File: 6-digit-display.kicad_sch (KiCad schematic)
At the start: 6 parts, among them U1 MAX7219, U2 3_digit_7_segment_display, U3 3_digit_7_segment_display

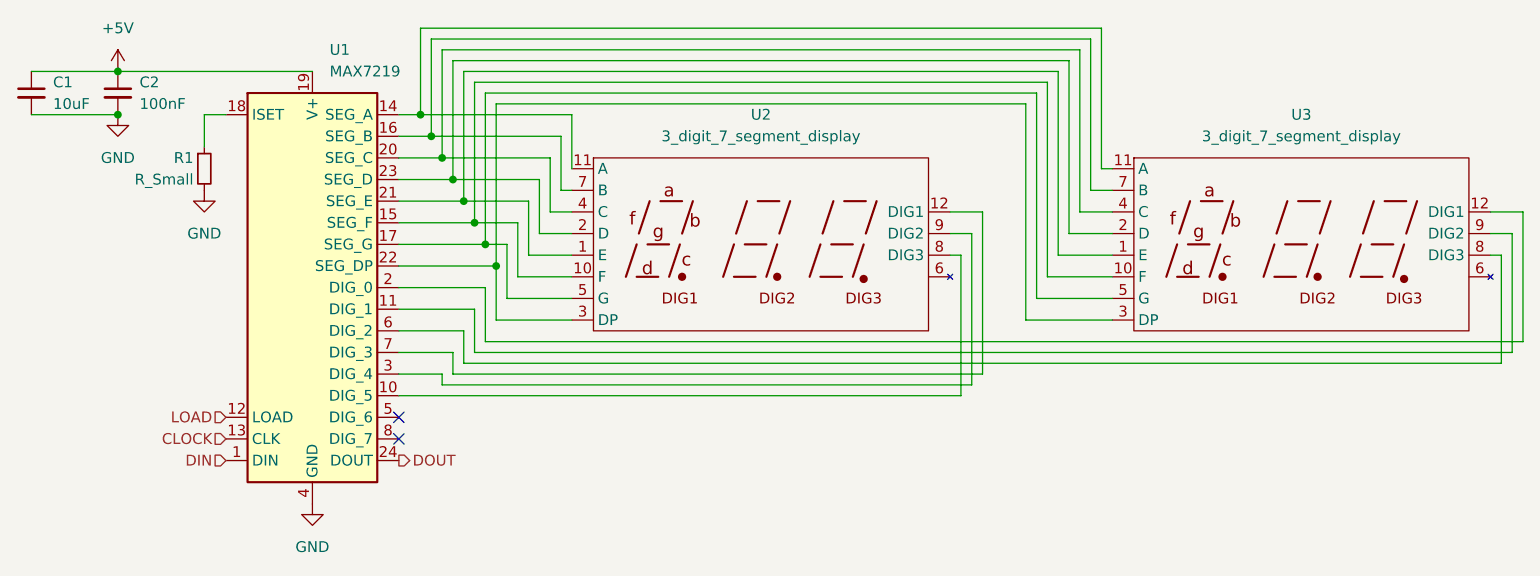
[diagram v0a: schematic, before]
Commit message: Add RP2040
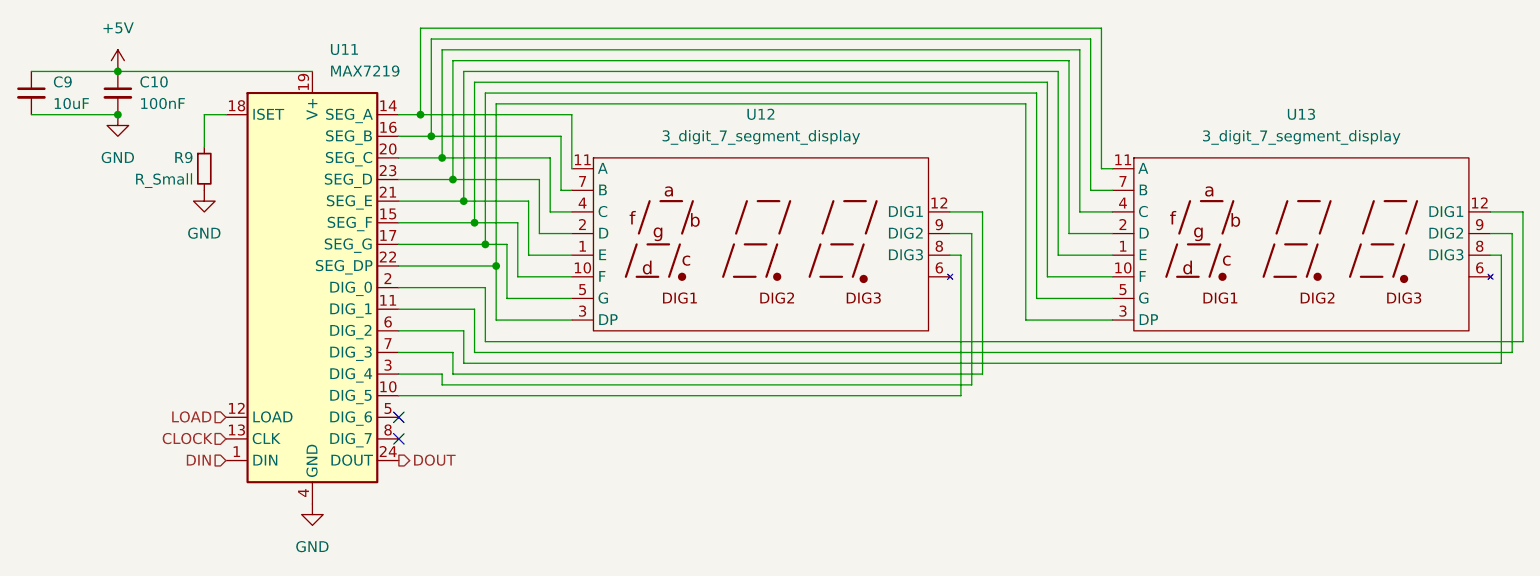
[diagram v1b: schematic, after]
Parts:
- renumbered C2 to C10, C1 to C9, R1 to R9, U1 to U11, U2 to U12, U3 to U13
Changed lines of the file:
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@@
   (symbol (lib_id "Driver_LED:MAX7219") (at 60.96 101.6 0)
     (in_bom yes) (on_board yes) (fields_autoplaced)
-    (property "Reference" "U1" (id 0) (at 62.9794 73.66 0)
+    (property "Reference" "U11" (id 0) (at 62.9794 73.66 0)
       (effects (font (size 1.27 1.27)) (justify left))
     )
@@
   (symbol (lib_id "Generic-radio-stack:3_digit_7_segment_display") (at 176.53 96.52 0)
     (in_bom yes) (on_board yes) (fields_autoplaced)
-    (property "Reference" "U3" (id 0) (at 177.165 81.28 0))
+    (property "Reference" "U13" (id 0) (at 177.165 81.28 0))
     (property "Value" "3_digit_7_segment_display" (id 1) (at 177.165 83.82 0))
     (property "Footprint" "" (id 2) (at 181.61 96.52 0)
@@
   (symbol (lib_id "Device:C_Small") (at 38.1 78.74 0)
     (in_bom yes) (on_board yes) (fields_autoplaced)
-    (property "Reference" "C2" (id 0) (at 40.64 77.4762 0)
+    (property "Reference" "C10" (id 0) (at 40.64 77.4762 0)
       (effects (font (size 1.27 1.27)) (justify left))
     )
@@
   (symbol (lib_id "power:GND") (at 38.1 81.28 0)
     (in_bom yes) (on_board yes) (fields_autoplaced)
-    (property "Reference" "#PWR014" (id 0) (at 38.1 87.63 0)
+    (property "Reference" "#PWR023" (id 0) (at 38.1 87.63 0)
       (effects (font (size 1.27 1.27)) hide)
     )
@@
   (symbol (lib_id "Device:R_Small") (at 48.26 87.63 0)
     (in_bom yes) (on_board yes)
-    (property "Reference" "R1" (id 0) (at 46.99 86.36 0)
+    (property "Reference" "R9" (id 0) (at 46.99 86.36 0)
       (effects (font (size 1.27 1.27)) (justify right))
     )
@@
   (symbol (lib_id "power:+5V") (at 38.1 76.2 0)
     (in_bom yes) (on_board yes) (fields_autoplaced)
-    (property "Reference" "#PWR013" (id 0) (at 38.1 80.01 0)
+    (property "Reference" "#PWR022" (id 0) (at 38.1 80.01 0)
       (effects (font (size 1.27 1.27)) hide)
     )
@@
   (symbol (lib_id "power:GND") (at 48.26 90.17 0)
     (in_bom yes) (on_board yes) (fields_autoplaced)
-    (property "Reference" "#PWR015" (id 0) (at 48.26 96.52 0)
+    (property "Reference" "#PWR024" (id 0) (at 48.26 96.52 0)
       (effects (font (size 1.27 1.27)) hide)
     )
@@
   (symbol (lib_id "power:GND") (at 60.96 127 0)
     (in_bom yes) (on_board yes) (fields_autoplaced)
-    (property "Reference" "#PWR016" (id 0) (at 60.96 133.35 0)
+    (property "Reference" "#PWR025" (id 0) (at 60.96 133.35 0)
       (effects (font (size 1.27 1.27)) hide)
     )
@@
   (symbol (lib_id "Device:C_Small") (at 27.94 78.74 0)
     (in_bom yes) (on_board yes) (fields_autoplaced)
-    (property "Reference" "C1" (id 0) (at 30.48 77.4762 0)
+    (property "Reference" "C9" (id 0) (at 30.48 77.4762 0)
       (effects (font (size 1.27 1.27)) (justify left))
     )
@@
   (symbol (lib_id "Generic-radio-stack:3_digit_7_segment_display") (at 113.03 96.52 0)
     (in_bom yes) (on_board yes) (fields_autoplaced)
-    (property "Reference" "U2" (id 0) (at 113.665 81.28 0))
+    (property "Reference" "U12" (id 0) (at 113.665 81.28 0))
     (property "Value" "3_digit_7_segment_display" (id 1) (at 113.665 83.82 0))
     (property "Footprint" "" (id 2) (at 118.11 96.52 0)

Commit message: Bunch more schematic work
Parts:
- C10: footprint (none) -> Capacitor_SMD:C_0805_2012Metric
- R13: renamed from R9; footprint (none) -> Resistor_SMD:R_0805_2012Metric
- U11: footprint (none) -> Package_SO:SOIC-24W_7.5x15.4mm_P1.27mm
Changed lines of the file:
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@@
       (effects (font (size 1.27 1.27)) (justify left))
     )
-    (property "Footprint" "" (id 2) (at 59.69 100.33 0)
+    (property "Footprint" "Package_SO:SOIC-24W_7.5x15.4mm_P1.27mm" (id 2) (at 59.69 100.33 0)
       (effects (font (size 1.27 1.27)) hide)
     )
@@
       (effects (font (size 1.27 1.27)) (justify left))
     )
-    (property "Footprint" "" (id 2) (at 38.1 78.74 0)
+    (property "Footprint" "Capacitor_SMD:C_0805_2012Metric" (id 2) (at 38.1 78.74 0)
       (effects (font (size 1.27 1.27)) hide)
     )
@@
   (symbol (lib_id "power:GND") (at 38.1 81.28 0)
     (in_bom yes) (on_board yes) (fields_autoplaced)
-    (property "Reference" "#PWR023" (id 0) (at 38.1 87.63 0)
+    (property "Reference" "#PWR025" (id 0) (at 38.1 87.63 0)
       (effects (font (size 1.27 1.27)) hide)
     )
@@
   (symbol (lib_id "Device:R_Small") (at 48.26 87.63 0)
     (in_bom yes) (on_board yes)
-    (property "Reference" "R9" (id 0) (at 46.99 86.36 0)
+    (property "Reference" "R13" (id 0) (at 46.99 86.36 0)
       (effects (font (size 1.27 1.27)) (justify right))
     )
@@
       (effects (font (size 1.27 1.27)) (justify right))
     )
-    (property "Footprint" "" (id 2) (at 48.26 87.63 0)
+    (property "Footprint" "Resistor_SMD:R_0805_2012Metric" (id 2) (at 48.26 87.63 0)
       (effects (font (size 1.27 1.27)) hide)
     )
@@
   (symbol (lib_id "power:+5V") (at 38.1 76.2 0)
     (in_bom yes) (on_board yes) (fields_autoplaced)
-    (property "Reference" "#PWR022" (id 0) (at 38.1 80.01 0)
+    (property "Reference" "#PWR024" (id 0) (at 38.1 80.01 0)
       (effects (font (size 1.27 1.27)) hide)
     )
@@
   (symbol (lib_id "power:GND") (at 48.26 90.17 0)
     (in_bom yes) (on_board yes) (fields_autoplaced)
-    (property "Reference" "#PWR024" (id 0) (at 48.26 96.52 0)
+    (property "Reference" "#PWR026" (id 0) (at 48.26 96.52 0)
       (effects (font (size 1.27 1.27)) hide)
     )
@@
   (symbol (lib_id "power:GND") (at 60.96 127 0)
     (in_bom yes) (on_board yes) (fields_autoplaced)
-    (property "Reference" "#PWR025" (id 0) (at 60.96 133.35 0)
+    (property "Reference" "#PWR027" (id 0) (at 60.96 133.35 0)
       (effects (font (size 1.27 1.27)) hide)
     )

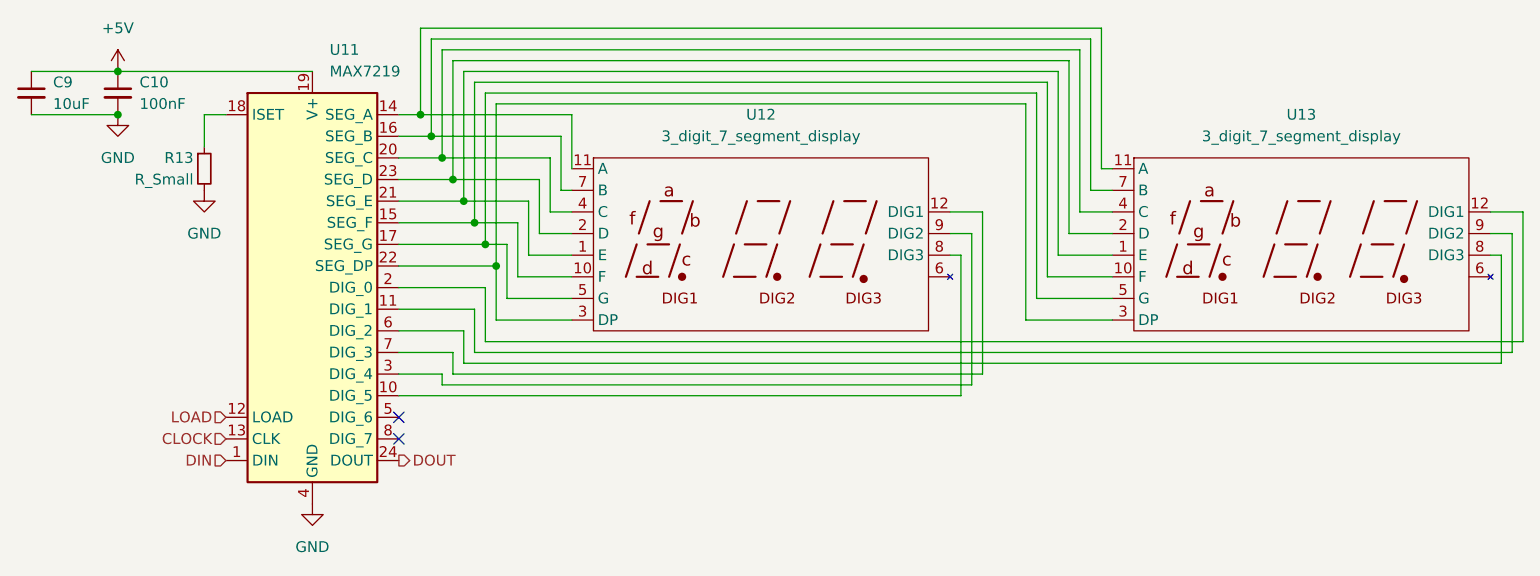
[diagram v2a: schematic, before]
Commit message: Add display footprints and models
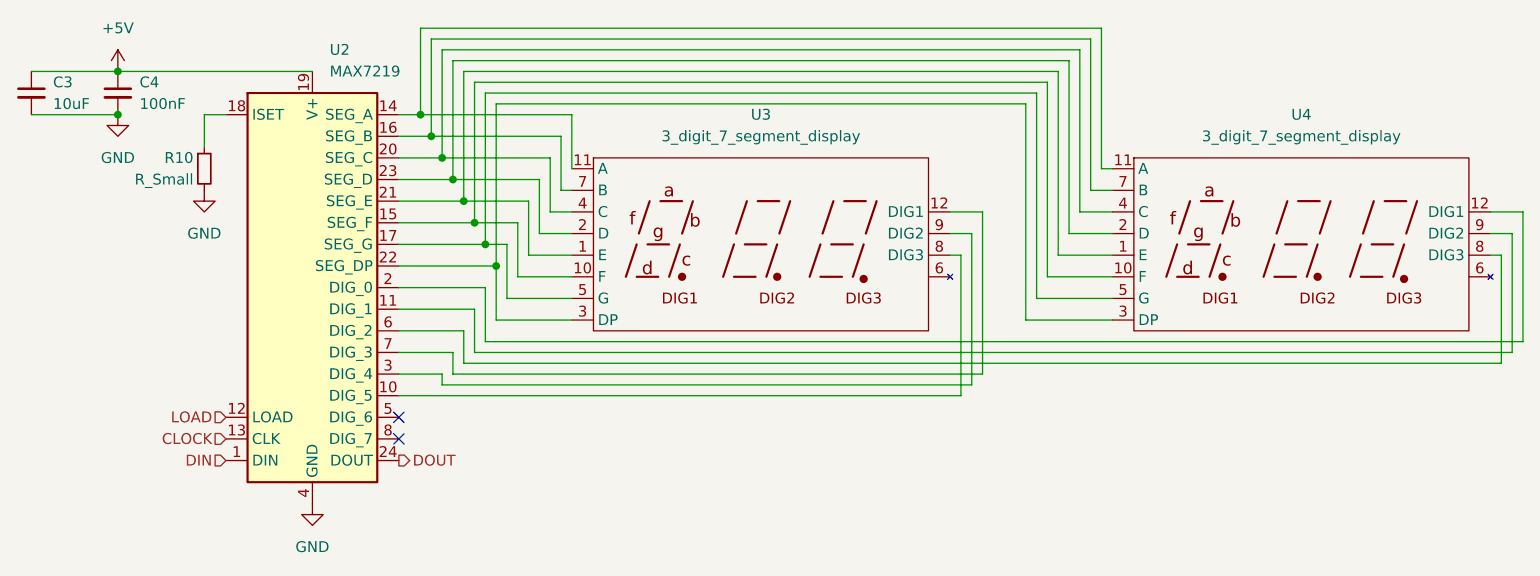
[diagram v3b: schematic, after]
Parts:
- C3: renamed from C9; footprint (none) -> Generic-radio-stack:Perfect_0402
- C4: renamed from C10; footprint Capacitor_SMD:C_0805_2012Metric -> Generic-radio-stack:Perfect_0402
- R10: renamed from R13; footprint Resistor_SMD:R_0805_2012Metric -> Generic-radio-stack:Perfect_0402
- renumbered U11 to U2, U12 to U3, U13 to U4
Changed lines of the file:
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@@
   (symbol (lib_id "Driver_LED:MAX7219") (at 60.96 101.6 0)
     (in_bom yes) (on_board yes) (fields_autoplaced)
-    (property "Reference" "U11" (id 0) (at 62.9794 73.66 0)
+    (property "Reference" "U2" (id 0) (at 62.9794 73.66 0)
       (effects (font (size 1.27 1.27)) (justify left))
     )
@@
   (symbol (lib_id "Generic-radio-stack:3_digit_7_segment_display") (at 176.53 96.52 0)
     (in_bom yes) (on_board yes) (fields_autoplaced)
-    (property "Reference" "U13" (id 0) (at 177.165 81.28 0))
+    (property "Reference" "U4" (id 0) (at 177.165 81.28 0))
     (property "Value" "3_digit_7_segment_display" (id 1) (at 177.165 83.82 0))
     (property "Footprint" "" (id 2) (at 181.61 96.52 0)
@@
   (symbol (lib_id "Device:C_Small") (at 38.1 78.74 0)
     (in_bom yes) (on_board yes) (fields_autoplaced)
-    (property "Reference" "C10" (id 0) (at 40.64 77.4762 0)
+    (property "Reference" "C4" (id 0) (at 40.64 77.4762 0)
       (effects (font (size 1.27 1.27)) (justify left))
     )
@@
       (effects (font (size 1.27 1.27)) (justify left))
     )
-    (property "Footprint" "Capacitor_SMD:C_0805_2012Metric" (id 2) (at 38.1 78.74 0)
+    (property "Footprint" "Generic-radio-stack:Perfect_0402" (id 2) (at 38.1 78.74 0)
       (effects (font (size 1.27 1.27)) hide)
     )
@@
   (symbol (lib_id "power:GND") (at 38.1 81.28 0)
     (in_bom yes) (on_board yes) (fields_autoplaced)
-    (property "Reference" "#PWR025" (id 0) (at 38.1 87.63 0)
+    (property "Reference" "#PWR013" (id 0) (at 38.1 87.63 0)
       (effects (font (size 1.27 1.27)) hide)
     )
@@
   (symbol (lib_id "Device:R_Small") (at 48.26 87.63 0)
     (in_bom yes) (on_board yes)
-    (property "Reference" "R13" (id 0) (at 46.99 86.36 0)
+    (property "Reference" "R10" (id 0) (at 46.99 86.36 0)
       (effects (font (size 1.27 1.27)) (justify right))
     )
@@
       (effects (font (size 1.27 1.27)) (justify right))
     )
-    (property "Footprint" "Resistor_SMD:R_0805_2012Metric" (id 2) (at 48.26 87.63 0)
+    (property "Footprint" "Generic-radio-stack:Perfect_0402" (id 2) (at 48.26 87.63 0)
       (effects (font (size 1.27 1.27)) hide)
     )
@@
   (symbol (lib_id "power:+5V") (at 38.1 76.2 0)
     (in_bom yes) (on_board yes) (fields_autoplaced)
-    (property "Reference" "#PWR024" (id 0) (at 38.1 80.01 0)
+    (property "Reference" "#PWR012" (id 0) (at 38.1 80.01 0)
       (effects (font (size 1.27 1.27)) hide)
     )
@@
   (symbol (lib_id "power:GND") (at 48.26 90.17 0)
     (in_bom yes) (on_board yes) (fields_autoplaced)
-    (property "Reference" "#PWR026" (id 0) (at 48.26 96.52 0)
+    (property "Reference" "#PWR014" (id 0) (at 48.26 96.52 0)
       (effects (font (size 1.27 1.27)) hide)
     )
@@
   (symbol (lib_id "power:GND") (at 60.96 127 0)
     (in_bom yes) (on_board yes) (fields_autoplaced)
-    (property "Reference" "#PWR027" (id 0) (at 60.96 133.35 0)
+    (property "Reference" "#PWR015" (id 0) (at 60.96 133.35 0)
       (effects (font (size 1.27 1.27)) hide)
     )
@@
   (symbol (lib_id "Device:C_Small") (at 27.94 78.74 0)
     (in_bom yes) (on_board yes) (fields_autoplaced)
-    (property "Reference" "C9" (id 0) (at 30.48 77.4762 0)
+    (property "Reference" "C3" (id 0) (at 30.48 77.4762 0)
       (effects (font (size 1.27 1.27)) (justify left))
     )
@@
       (effects (font (size 1.27 1.27)) (justify left))
     )
-    (property "Footprint" "" (id 2) (at 27.94 78.74 0)
+    (property "Footprint" "Generic-radio-stack:Perfect_0402" (id 2) (at 27.94 78.74 0)
       (effects (font (size 1.27 1.27)) hide)
     )
@@
   (symbol (lib_id "Generic-radio-stack:3_digit_7_segment_display") (at 113.03 96.52 0)
     (in_bom yes) (on_board yes) (fields_autoplaced)
-    (property "Reference" "U12" (id 0) (at 113.665 81.28 0))
+    (property "Reference" "U3" (id 0) (at 113.665 81.28 0))
     (property "Value" "3_digit_7_segment_display" (id 1) (at 113.665 83.82 0))
     (property "Footprint" "" (id 2) (at 118.11 96.52 0)

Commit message: Custom component for six digit display
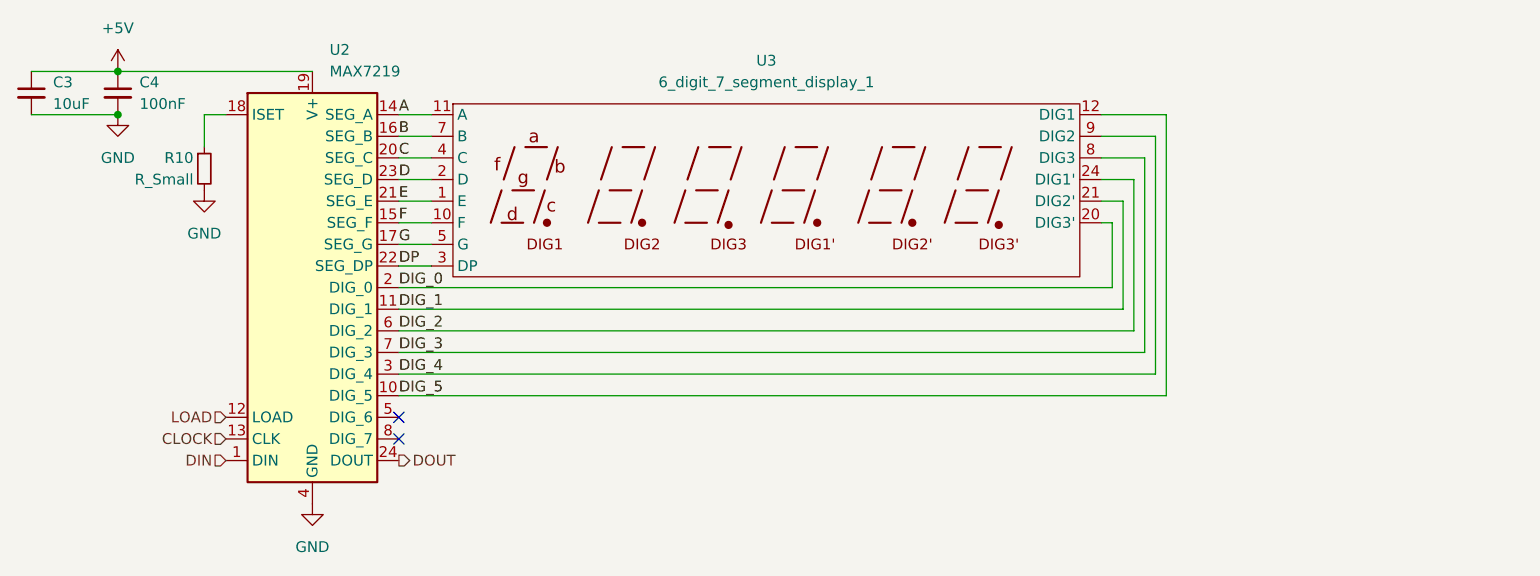
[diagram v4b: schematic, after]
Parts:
- removed U3, U4: 3_digit_7_segment_display, symbol Generic-radio-stack:3_digit_7_segment_display
- added U3: 6_digit_7_segment_display_1, Generic-radio-stack:6 digit (3x2) 7 segment LED display, symbol Generic-radio-stack:6_digit_7_segment_display_1
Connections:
- net DIG_5: now reaches U2.10 (DIG_5)
- net DIG_5: now also U3.12 (DIG1)
- net DIG_1: now reaches U2.11 (DIG_1)
- net DIG_1: now also U3.21 (DIG2')
- net A: now reaches U2.14 (SEG_A)
- net A: now also U3.11 (A), U3.23 (A')
- net F: now reaches U2.15 (SEG_F)
- net F: now also U3.10 (F), U3.22 (F')
- net B: now reaches U2.16 (SEG_B)
- net B: now also U3.19 (B'), U3.7 (B)
- net G: now reaches U2.17 (SEG_G)
- net G: now also U3.17 (G'), U3.5 (G)
- net DIG_0: now reaches U2.2 (DIG_0)
- net DIG_0: now also U3.20 (DIG3')
- net C: now reaches U2.20 (SEG_C)
- net C: now also U3.16 (C'), U3.4 (C)
- net E: now reaches U2.21 (SEG_E)
- net E: now also U3.1 (E), U3.13 (E')
- net DP: now reaches U2.22 (SEG_DP)
- net DP: now also U3.15 (DP'), U3.3 (DP)
- net D: now reaches U2.23 (SEG_D)
- net D: now also U3.14 (D'), U3.2 (D)
- net DIG_4: now reaches U2.3 (DIG_4)
- net DIG_4: now also U3.9 (DIG2)
- net DIG_2: now reaches U2.6 (DIG_2)
- net DIG_2: now also U3.24 (DIG1')
- net DIG_3: now reaches U2.7 (DIG_3)
- net DIG_3: now also U3.8 (DIG3)
